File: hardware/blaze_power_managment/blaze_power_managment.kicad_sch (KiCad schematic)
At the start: 33 parts, among them J1 XT30, Q1 PMOS

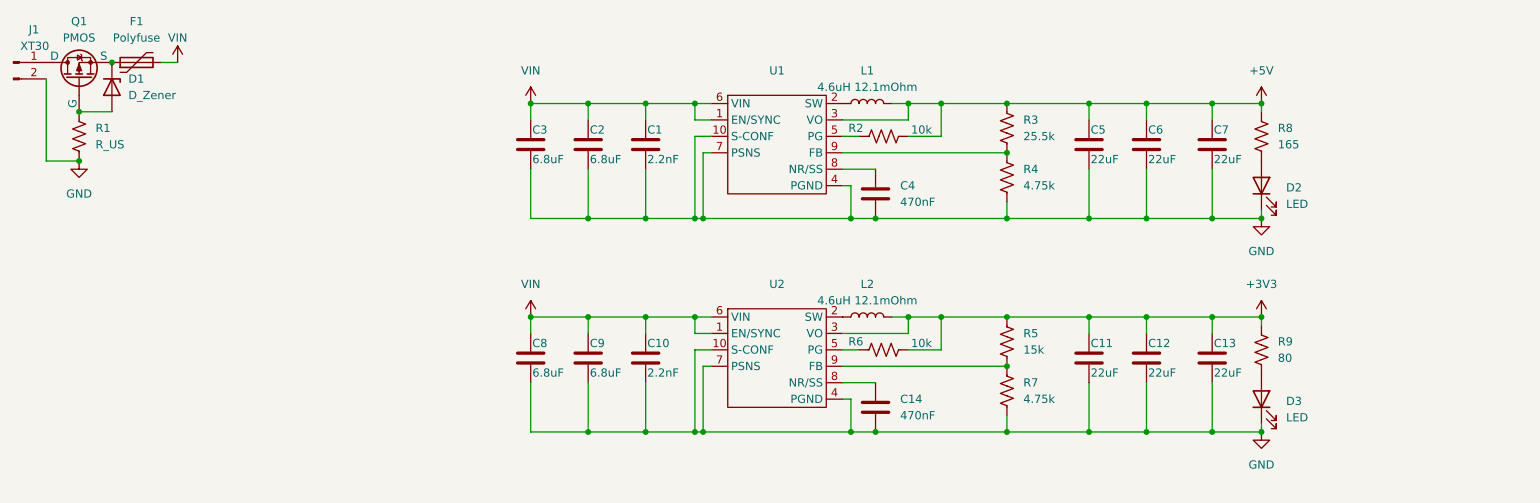
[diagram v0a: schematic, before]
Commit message: Moved main power function to power management
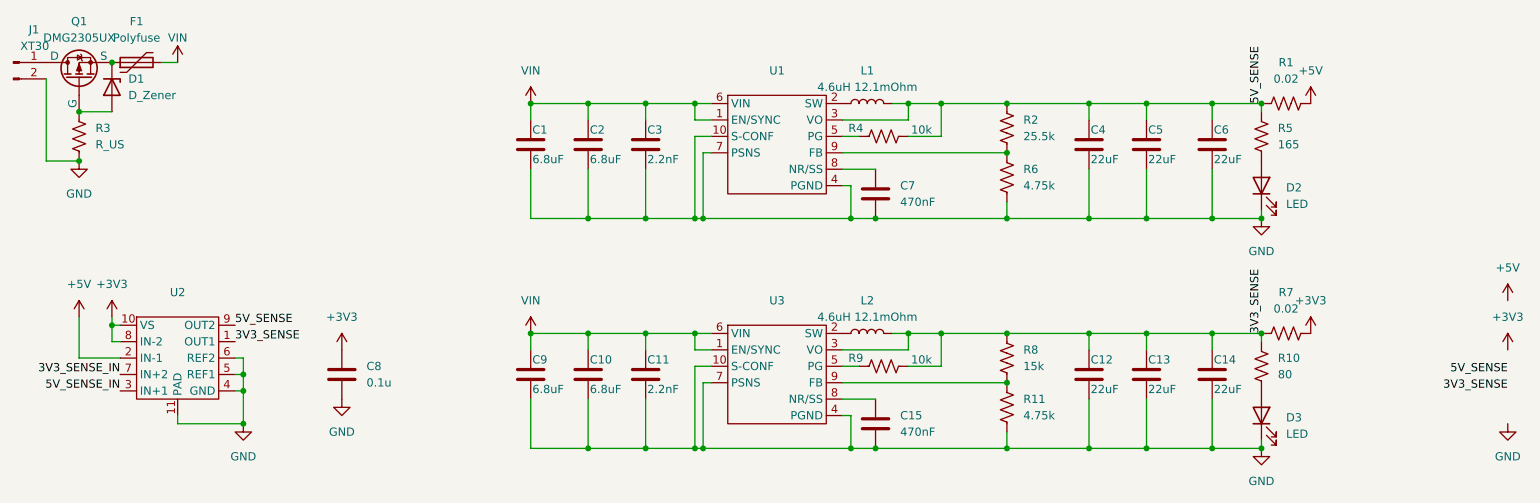
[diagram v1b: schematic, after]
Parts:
- added C8: 0.1u, symbol Device:C
- added R1, R7: 0.02, symbol Device:R_US
- added U2: ~, symbol Blaze_Lib:INA2181
- Q1: value PMOS -> DMG2305UX
- renumbered C3 to C1, C9 to C10, C10 to C11, C11 to C12, C12 to C13, C13 to C14, C14 to C15, C1 to C3, C5 to C4, C6 to C5, C7 to C6, C4 to C7, C8 to C9, R9 to R10, R7 to R11, R3 to R2, R1 to R3, R2 to R4, R8 to R5, R4 to R6, R5 to R8, R6 to R9, U2 to U3
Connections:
- net +3V3: now also C8.1, R7.2, U2.10 (VS), U2.8 (IN-2); no longer C12.1, C13.1, C14.1, L2.2, R10.1, R8.1, R9.2, U3.3 (VO)
- net +5V: now also R1.2, U2.2 (IN-1); no longer C4.1, C5.1, C6.1, L1.2, R2.1, R4.2, R5.1, U1.3 (VO)
- net GND: now also C8.2, U2.11 (PAD), U2.4 (GND), U2.5 (REF1), U2.6 (REF2)
- new net 3V3_SENSE: C12.1, C13.1, C14.1, L2.2, R10.1, R7.1, R8.1, R9.2, U2.1 (OUT1), U3.3 (VO)
- new net 3V3_SENSE_IN: U2.7 (IN+2)
- new net 5V_SENSE: C4.1, C5.1, C6.1, L1.2, R1.1, R2.1, R4.2, R5.1, U1.3 (VO), U2.9 (OUT2)
- new net 5V_SENSE_IN: U2.3 (IN+1)
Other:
- company: (none) -> UCSC Rocket Team
- title: (none) -> Blaze Power Managment
- moved on the sheet: C10, C11, C12, C13, C14, C15, C9, D3, L2, R10, R11, R8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

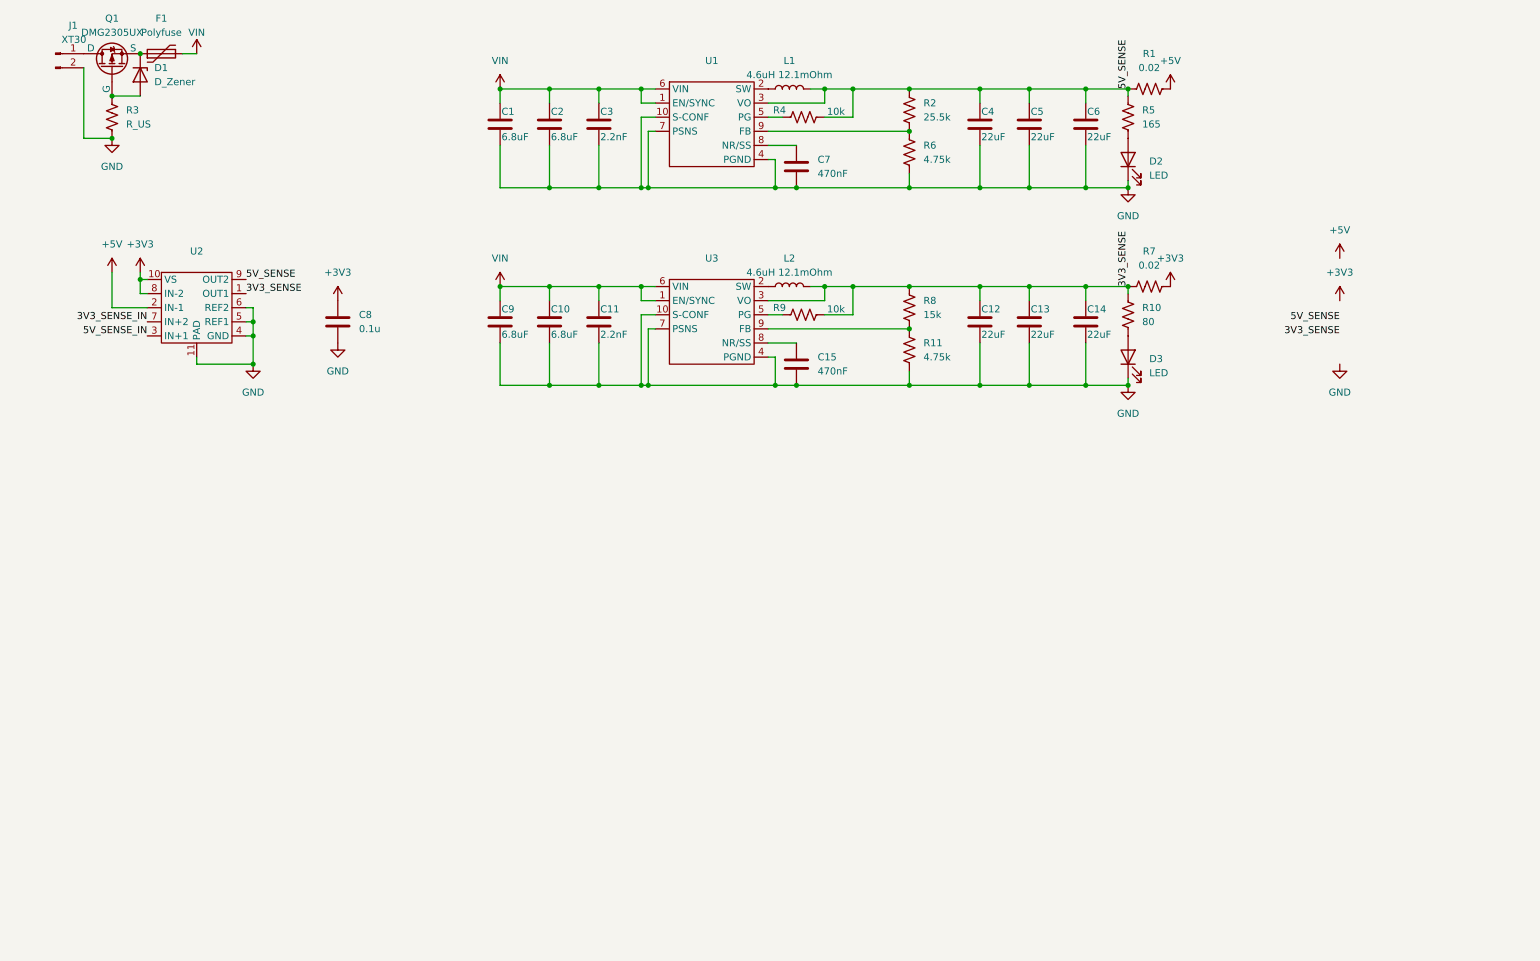
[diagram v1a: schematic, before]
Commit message: Created blaze sense, updated brain
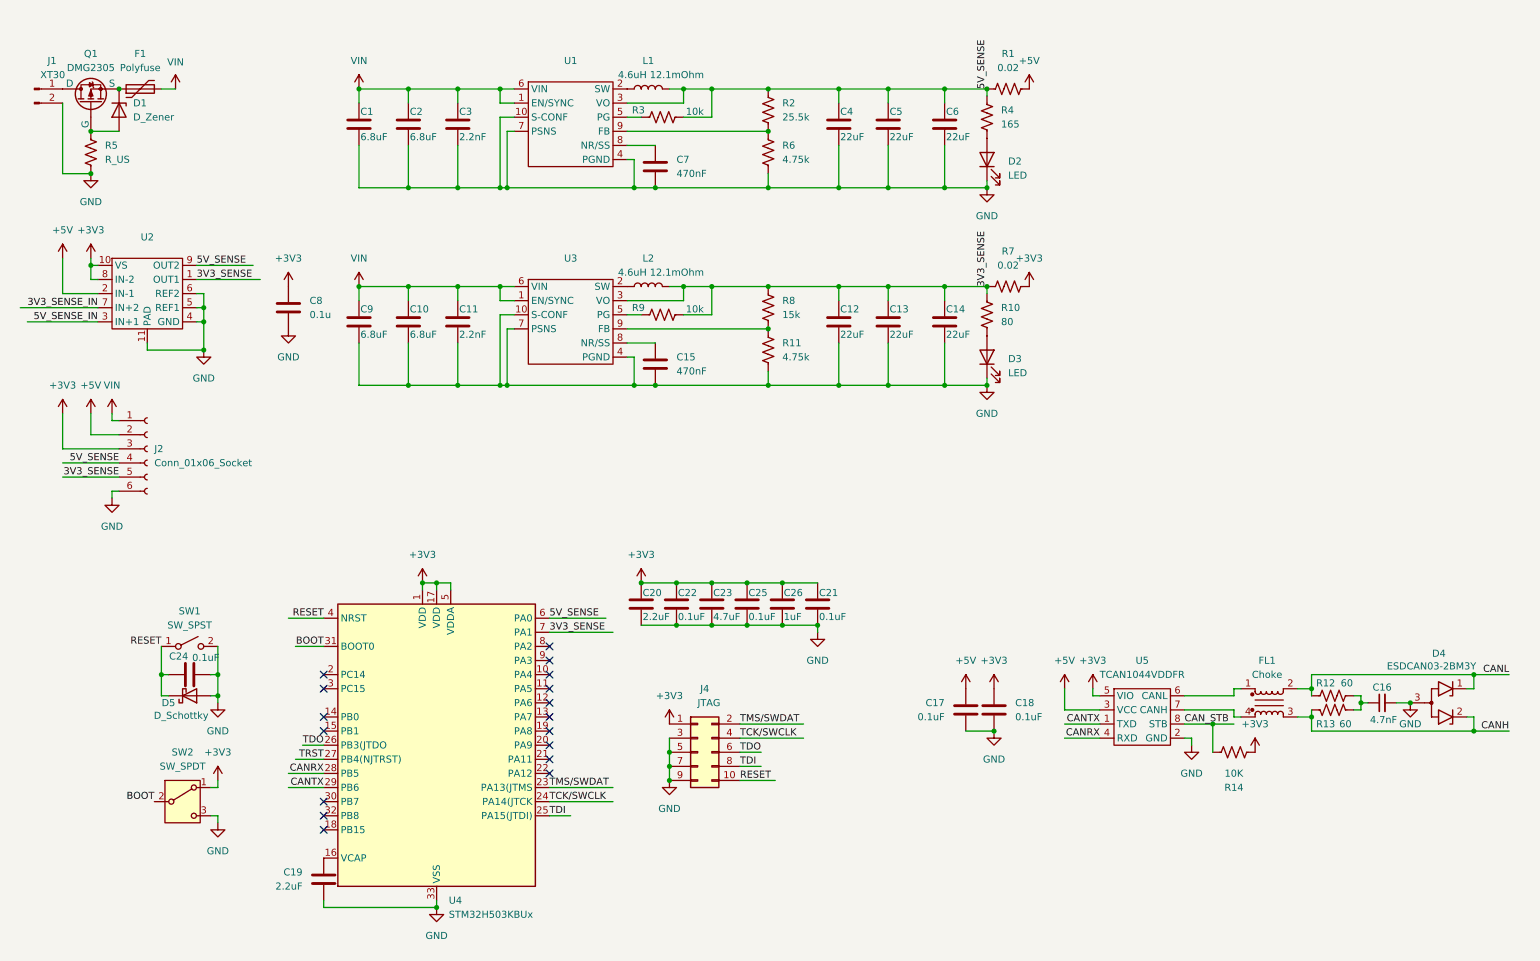
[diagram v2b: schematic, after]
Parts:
- added C16: 4.7nF, symbol Device:C_Small
- added C17, C18, C21, C22, C24, C25: 0.1uF, symbol Device:C
- added C19, C20: 2.2uF, symbol Device:C
- added C23: 4.7uF, symbol Device:C
- added C26: 1uF, symbol Device:C
- added D4: ESDCAN03-2BM3Y, Package_TO_SOT_SMD:SOT-416, symbol Power_Protection:RCLAMP0582B
- added D5: D_Schottky, symbol Device:D_Schottky
- added FL1: Choke, Inductor_SMD:L_CommonModeChoke_Coilcraft_0603USB, symbol Filter:Choke_Coilcraft_0603USB-142
- added J2: Conn_01x06_Socket, symbol Connector:Conn_01x06_Socket
- added J4: JTAG, symbol Connector_Generic:Conn_02x05_Odd_Even
- added R12, R13: 60, symbol Device:R_US
- added R14: 10K, symbol Device:R_US
- added SW1: SW_SPST, symbol Switch:SW_SPST
- added SW2: SW_SPDT, symbol Switch:SW_SPDT
- added U4: STM32H503KBUx, Package_DFN_QFN:QFN-32-1EP_5x5mm_P0.5mm_EP3.45x3.45mm, symbol MCU_ST_STM32H5:STM32H503KBUx
- added U5: TCAN1044VDDFR, symbol Blaze_Lib:TCAN1044
- Q1: value DMG2305UX -> DMG2305
- renumbered R4 to R3, R5 to R4, R3 to R5
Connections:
- net +3V3: now also C18.1, C20.1, C21.1, C22.1, C23.1, C25.1, C26.1, J2.3 (Pin_3), J4.1 (Pin_1), R14.2, SW2.1 (A), U4.1 (VDD), U4.17 (VDD), U4.5 (VDDA), U5.5 (VIO)
- net +5V: now also C17.1, J2.2 (Pin_2), U5.3 (VCC)
- net 3V3_SENSE: now also J2.5 (Pin_5), U4.7 (PA1)
- net 5V_SENSE: now also J2.4 (Pin_4), U4.6 (PA0)
- net GND: now also C16.2, C17.2, C18.2, C19.2, C20.2, C21.2, C22.2, C23.2, C24.2, C25.2, C26.2, D4.3 (A), D5.2 (A), J2.6 (Pin_6), J4.3 (Pin_3), J4.5 (Pin_5), J4.7 (Pin_7), J4.9 (Pin_9), SW1.2 (B), SW2.3 (C), U4.33 (VSS), U5.2 (GND)
- net VIN: now also J2.1 (Pin_1)
- new net: C16.1, R12.2, R13.2
- new net: FL1.1, U5.6 (CANL)
- new net: FL1.4, U5.7 (CANH)
- new net: C19.1, U4.16 (VCAP)
- new net BOOT: SW2.2 (B), U4.31 (BOOT0)
- new net CANH: D4.2 (K2), FL1.3, R13.1
- new net CANL: D4.1 (K1), FL1.2, R12.1
- new net CANRX: U4.28 (PB5), U5.4 (RXD)
- new net CANTX: U4.29 (PB6), U5.1 (TXD)
- new net CAN_STB: R14.1, U5.8 (STB)
- new net RESET: C24.1, D5.1 (K), J4.10 (Pin_10), SW1.1 (A), U4.4 (NRST)
- new net TCK/SWCLK: J4.4 (Pin_4), U4.24 (PA14(JTCK)
- new net TDI: J4.8 (Pin_8), U4.25 (PA15(JTDI))
- new net TDO: J4.6 (Pin_6), U4.26 (PB3(JTDO)
- new net TMS/SWDAT: J4.2 (Pin_2), U4.23 (PA13(JTMS)
- new net TRST: U4.27 (PB4(NJTRST))
- no-connect marks 0 -> 17
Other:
- moved on the sheet: C1, C10, C11, C12, C13, C14, C15, C2, C3, C4, C5, C6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

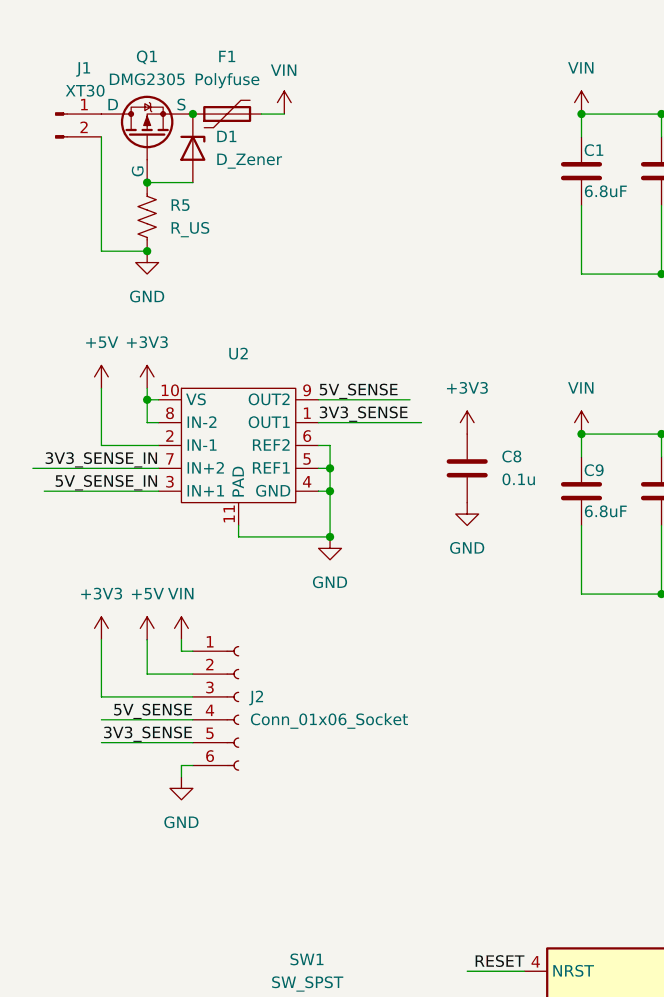
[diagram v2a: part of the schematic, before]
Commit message: Created blaze io
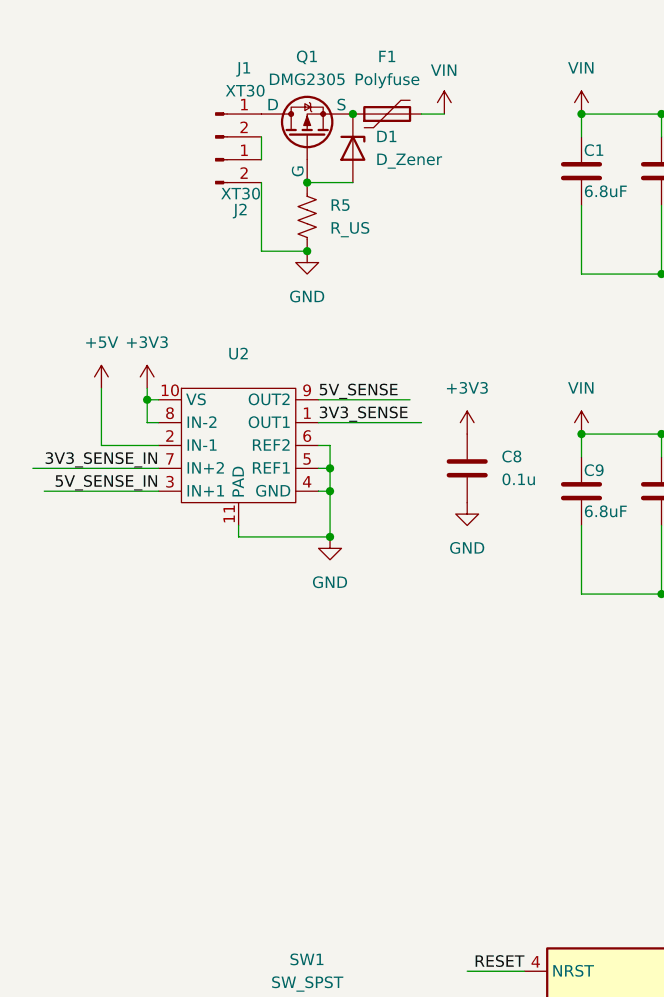
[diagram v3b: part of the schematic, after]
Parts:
- removed J2: Conn_01x06_Socket, symbol Connector:Conn_01x06_Socket
- added J2: XT30, symbol Connector:Conn_01x02_Pin
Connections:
- net GND: now also J2.2 (Pin_2); no longer J1.2 (Pin_2)
- new net: J1.2 (Pin_2), J2.1 (Pin_1)
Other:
- moved on the sheet: D1, F1, J1, Q1, R5

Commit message: Connected IO, wrote docs
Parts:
- C8: value 0.1u -> 0.1uF

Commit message: Removed audio, neopixel, can2 from interconnect
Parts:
- added J3: Conn_01x30, symbol Connector_Generic:Conn_01x30
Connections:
- net +3V3: now also J3.12 (Pin_12), J3.18 (Pin_18), J3.29 (Pin_29), J3.30 (Pin_30)
- net +5V: now also J3.11 (Pin_11), J3.27 (Pin_27), J3.28 (Pin_28)
- net CANH: now also J3.24 (Pin_24)
- net CANL: now also J3.23 (Pin_23)
- net GND: now also J3.14 (Pin_14), J3.15 (Pin_15), J3.21 (Pin_21), J3.22 (Pin_22), J3.3 (Pin_3), J3.4 (Pin_4)
- net PPS: now reaches U4.18 (PB15)
- net PPS: now also J3.13 (Pin_13)
- new net ARM: J3.8 (Pin_8)
- new net VBATT: J3.1 (Pin_1), J3.2 (Pin_2)
- no-connect marks 17 -> 27

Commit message: PowerMan Footprint Assignments
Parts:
- C1, C10, C11, C12, C13, C14, C15, C16, C17, C18, C19, C2, C20, C21, C22, C23, C24, C25, C26, C3, C4, C5, C6, C7, C8, C9: footprint (none) -> Capacitor_SMD:C_0603_1608Metric
- D2, D3: footprint (none) -> LED_SMD:LED_0603_1608Metric
- D5: footprint (none) -> Diode_SMD:D_0603_1608Metric
- J3: footprint (none) -> DF17:HRS_DF17_1.0H_-30DP-0.5V_57_
- J4: footprint (none) -> Connector_PinHeader_1.00mm:PinHeader_2x05_P1.00mm_Vertical_SMD
- R1, R10, R11, R12, R13, R14, R2, R3, R4, R5, R6, R7, R8, R9: footprint (none) -> Resistor_SMD:R_0603_1608Metric
- SW1: footprint (none) -> Button_Switch_SMD:SW_SPST_B3U-1000P
- SW2: footprint (none) -> Button_Switch_SMD:Nidec_Copal_CAS-120A
- U5: footprint (none) -> Package_SON:Texas_VSON-HR-8_1.5x2mm_P0.5mm

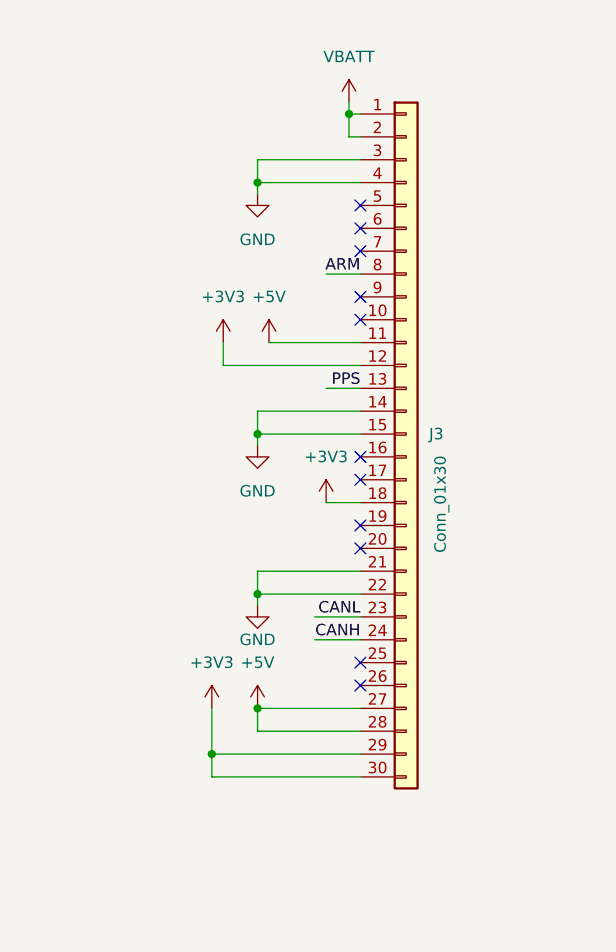
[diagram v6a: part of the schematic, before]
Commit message: Added mirror interconnect and PCB to gps
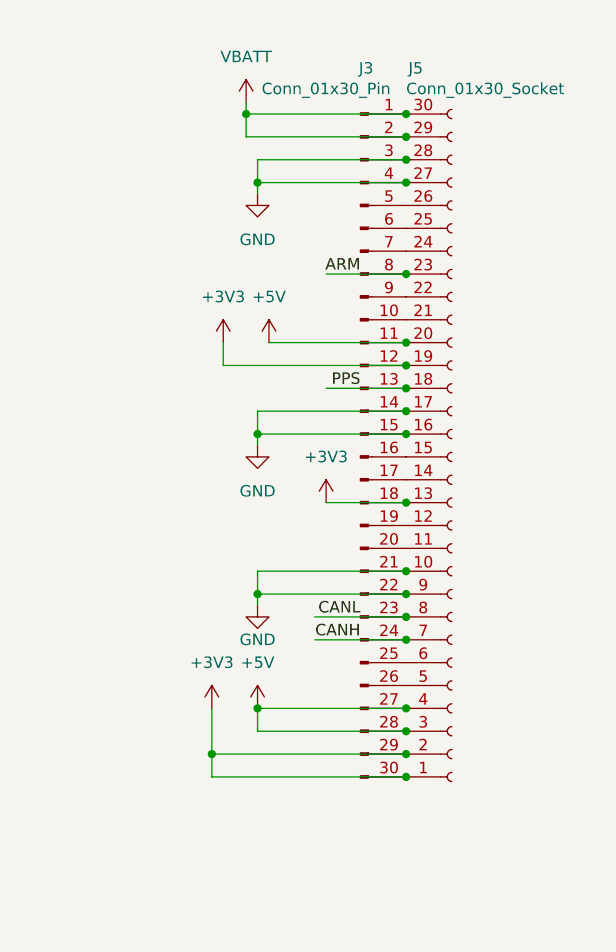
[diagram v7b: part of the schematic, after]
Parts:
- removed J3: Conn_01x30, DF17:HRS_DF17_1.0H_-30DP-0.5V_57_, symbol Connector_Generic:Conn_01x30
- added J3: Conn_01x30_Pin, Blaze_Library:HRS_DF17_1.0H_-30DP-0.5V_57_, symbol Connector:Conn_01x30_Pin
- added J5: Conn_01x30_Socket, Blaze_Library:HRS_DF17_1.0H_-30DP-0.5V_57_, symbol Connector:Conn_01x30_Socket
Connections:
- net +3V3: now also J3.12 (Pin_12), J3.18 (Pin_18), J3.29 (Pin_29), J3.30 (Pin_30), J5.1 (Pin_1), J5.13 (Pin_13), J5.19 (Pin_19), J5.2 (Pin_2)
- net +5V: now also J3.11 (Pin_11), J3.27 (Pin_27), J3.28 (Pin_28), J5.20 (Pin_20), J5.3 (Pin_3), J5.4 (Pin_4)
- net ARM: now also J3.8 (Pin_8), J5.23 (Pin_23)
- net CANH: now also J3.24 (Pin_24), J5.7 (Pin_7)
- net CANL: now also J3.23 (Pin_23), J5.8 (Pin_8)
- net GND: now also J3.14 (Pin_14), J3.15 (Pin_15), J3.21 (Pin_21), J3.22 (Pin_22), J3.3 (Pin_3), J3.4 (Pin_4), J5.10 (Pin_10), J5.16 (Pin_16), J5.17 (Pin_17), J5.27 (Pin_27), J5.28 (Pin_28), J5.9 (Pin_9)
- net PPS: now also J3.13 (Pin_13), J5.18 (Pin_18)
- net VBATT: now also J3.1 (Pin_1), J3.2 (Pin_2), J5.29 (Pin_29), J5.30 (Pin_30)
- new net: J3.10 (Pin_10), J5.21 (Pin_21)
- new net: J3.16 (Pin_16), J5.15 (Pin_15)
- new net: J3.17 (Pin_17), J5.14 (Pin_14)
- new net: J3.19 (Pin_19), J5.12 (Pin_12)
- new net: J3.20 (Pin_20), J5.11 (Pin_11)
- new net: J3.25 (Pin_25), J5.6 (Pin_6)
- new net: J3.26 (Pin_26), J5.5 (Pin_5)
- new net: J3.5 (Pin_5), J5.26 (Pin_26)
- new net: J3.6 (Pin_6), J5.25 (Pin_25)
- new net: J3.7 (Pin_7), J5.24 (Pin_24)
- new net: J3.9 (Pin_9), J5.22 (Pin_22)
- no-connect marks 27 -> 16

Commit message: Component assingment
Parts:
- D2: renamed from D1; footprint (none) -> Diode_SMD:D_0603_1608Metric
- F1: footprint (none) -> Fuse:Fuse_1206_3216Metric
- J3: renamed from J1; footprint (none) -> Connector_AMASS:AMASS_XT30PW-M_1x02_P2.50mm_Horizontal
- J4: renamed from J2; footprint (none) -> Connector_AMASS:AMASS_XT30PW-M_1x02_P2.50mm_Horizontal
- L1, L2: footprint (none) -> Inductor_SMD:L_SXN_SMDRI124
- Q1: footprint (none) -> Package_TO_SOT_SMD:SOT-23-3
- U2: renamed from U1; value ~ -> TPS62913; footprint (none) -> Blaze_Library:TPS62913R
- U3: renamed from U2; value ~ -> INA2181; footprint (none) -> Blaze_Library:WSON10-DSQ0010A_TEX
- U4: renamed from U3; value ~ -> TPS62913; footprint (none) -> Blaze_Library:TPS62913R
- renumbered C16 to C1, C7 to C10, C8 to C11, C9 to C12, C10 to C13, C11 to C14, C12 to C15, C13 to C16, C14 to C17, C15 to C18, C20 to C19, C17 to C2, C22 to C20, C23 to C21, C25 to C22, C26 to C23, C21 to C24, C24 to C25, C19 to C26, C18 to C3, C1 to C4, C2 to C5, C3 to C6, C4 to C7, C5 to C8, C6 to C9, D4 to D1, D2 to D3, D3 to D4, J3 to J1, J5 to J2, J4 to J5, R12 to R1, R7 to R10, R8 to R11, R9 to R12, R10 to R13, R11 to R14, R13 to R2, R14 to R3, R1 to R4, R2 to R5, R3 to R6, R4 to R7, R5 to R8, R6 to R9, U5 to U1, U4 to U5
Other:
- moved on the sheet: C10, C11, C12, C13, C14, C15, C16, C17, C18, C19, C20, C21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
